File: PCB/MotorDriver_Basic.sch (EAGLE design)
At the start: 20 parts, among them J2 MTR_CTRL, J3 MCU PWR, J4 MTR PWR

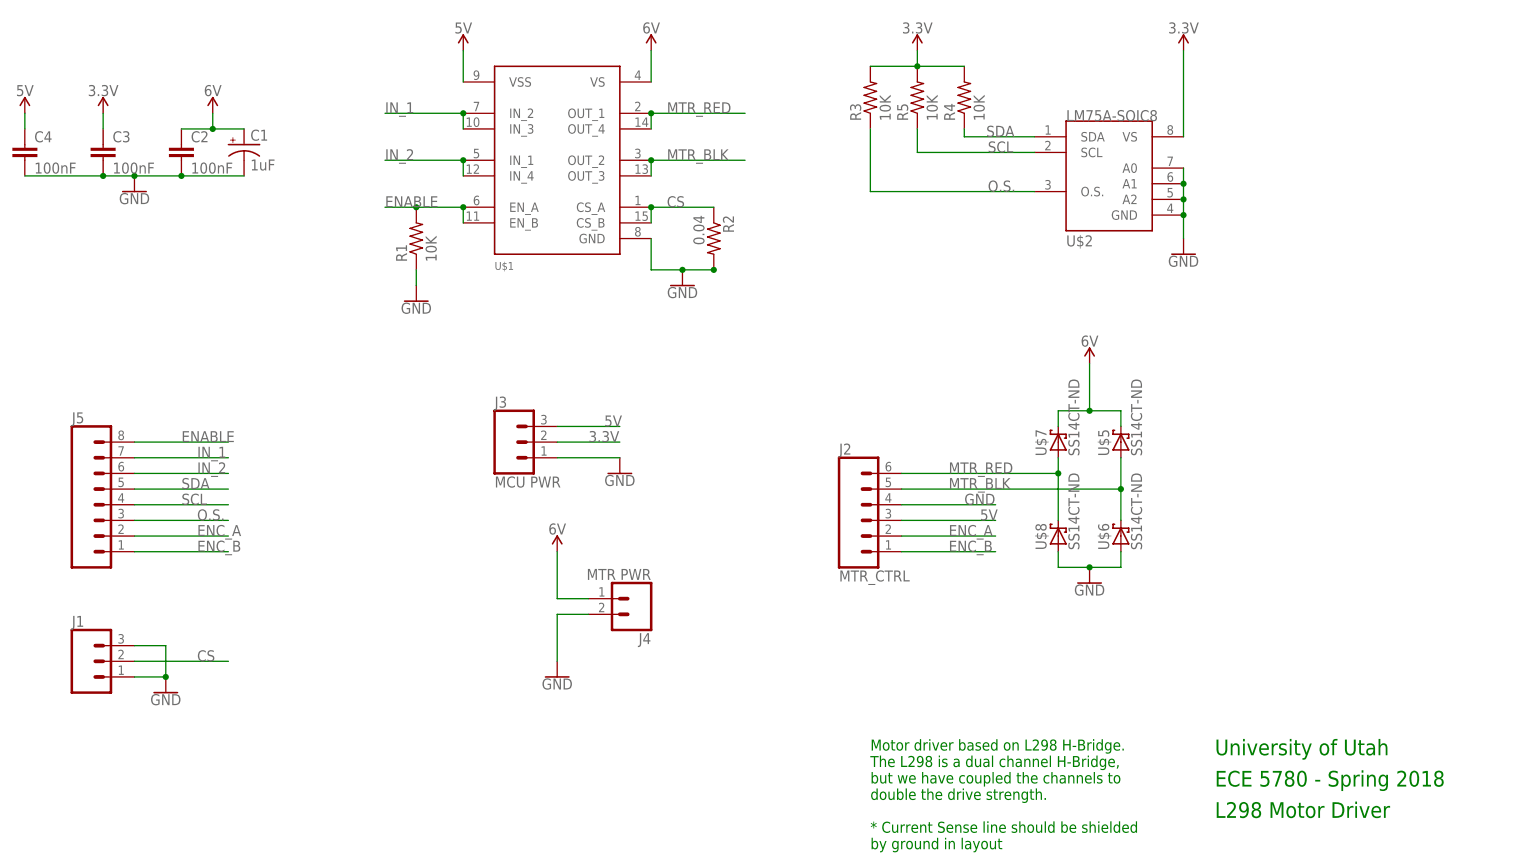
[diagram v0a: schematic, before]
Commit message: added the motor driver to schematic.
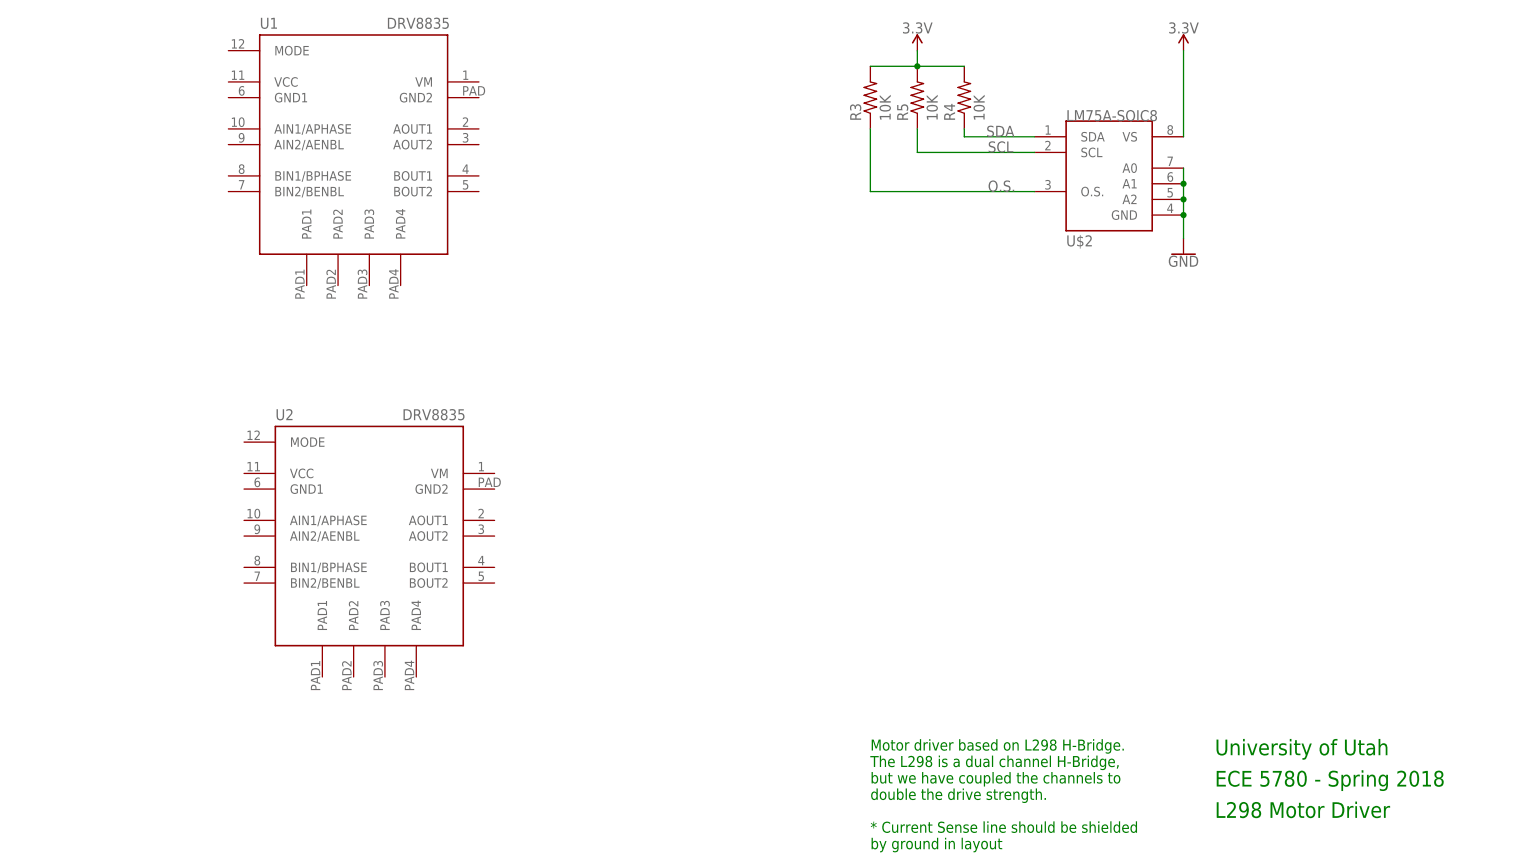
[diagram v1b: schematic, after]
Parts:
- removed C1: 1uF, rcl:CPOL-USE2.5-6
- removed C2, C3, C4: 100nF, rcl:C-EUC1206
- removed J1: (no value), SparkFun-Connectors:CONN_03
- removed J2: MTR_CTRL, SparkFun-Connectors:CONN_06SILK_FEMALE_PTH
- removed J3: MCU PWR, SparkFun-Connectors:CONN_03
- removed J4: MTR PWR, L298_Motor_Driver_Lib_ECE5780:CONN2-5MM-SCREW-TERM
- removed J5: (no value), SparkFun-Connectors:CONN_08"
- removed R1: 10K, rcl:R-US_M1206
- removed R2: 0.04, rcl:R-US_M1206
- removed U$1: L298N-MULTIWATT15, ECE5780-MotorDriver:L298N-MULTIWATT15
- removed U$5, U$6, U$7, U$8: SS14CT-ND, L298_Motor_Driver_Lib_ECE5780:SS14CT-ND
- added U1, U2: DRV8835, bt_motordriver:DRV8835
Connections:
- removed net 5V: C4.1, J2.3, J3.3, U$1.VSS
- removed net CS: J1.2, R2.1, U$1.CS_A, U$1.CS_B
- removed net ENABLE: J5.8, R1.2, U$1.EN_A, U$1.EN_B
- removed net ENC_A: J2.2, J5.2
- removed net ENC_B: J2.1, J5.1
- removed net IN_1: J5.7, U$1.IN_2, U$1.IN_3
- removed net IN_2: J5.6, U$1.IN_1, U$1.IN_4
- removed net MTR_BLK: J2.5, U$1.OUT_2, U$1.OUT_3, U$5.A, U$6.C
- removed net MTR_RED: J2.6, U$1.OUT_1, U$1.OUT_4, U$7.A, U$8.C
- removed net VCC: C1.+, C2.1, J4.1, U$1.VS, U$5.C, U$7.C
- net 3.3V: no longer C3.1, J3.2
- net GND: no longer C1.-, C2.2, C3.2, C4.2, J1.1, J1.3, J2.4, J3.1, J4.2, R1.1, R2.2, U$1.GND, U$6.A, U$8.A
- net O.S.: no longer J5.3
- net SCL: no longer J5.4
- net SDA: no longer J5.5

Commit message: Finished the Schematic.
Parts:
- removed U2: DRV8835, bt_motordriver:DRV8835
- added C1, C2, C3, C5: 0.1 uF, rcl:C-EUC1206
- added C4: 2.2 nF, rcl:C-EUC1206
- added C6: 1.0 uF, rcl:C-US025-050X050
- added C7: 10 nF, rcl:C-EUC1206
- added IC1: MPU6050, invensense:MPU6050
- added JP1, JP2: (no value), pinhead:PINHD-1X8
- added R1: 0, rcl:R-US_M1206
- added R2: 10K, rcl:R-US_M1206
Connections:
- removed net 3.3V: R3.2, R4.2, R5.2, U$2.VS
- new net AIN1: JP2.1, U1.AIN1/APHASE
- new net AIN2: JP2.2, U1.AIN2/AENBL
- new net BIN1: JP2.3, U1.BIN1/BPHASE
- new net BIN2: JP2.4, U1.BIN2/BENBL
- new net IMU_INT: JP1.3, R1.2, R2.1
- new net MOUTA1: JP2.8, U1.AOUT1
- new net MOUTA2: JP2.7, U1.AOUT2
- new net MOUTB1: JP1.8, U1.BOUT1
- new net MOUTB2: JP1.7, U1.BOUT2
- new net N$1: C4.1, IC1G$1.CPOUT
- new net N$2: IC1G$1.INT, R1.1
- new net REGOUT: C2.1, IC1G$1.REGOUT
- new net VCC: C3.1, C7.1, IC1G$1.VLOGIC, JP2.6, R2.2, R3.2, R4.2, R5.2, U$2.VS, U1.VCC
- new net VM: C1.1, C5.1, C6.1, IC1G$1.VDD, JP2.5, U1.VM
- net GND: now also C1.2, C2.2, C3.2, C4.2, C5.2, C6.2, C7.2, IC1G$1.AD0, IC1G$1.AUX_CL, IC1G$1.AUX_DA, IC1G$1.CLKIN, IC1G$1.FSYNC, IC1G$1.GND, IC1G$1.GND@1, JP1.1, JP1.2, JP1.4, U1.GND1, U1.GND2, U1.MODE, U1.PAD1, U1.PAD2, U1.PAD3, U1.PAD4
- net SCL: now also IC1G$1.SCL, JP1.6
- net SDA: now also IC1G$1.SDA, JP1.5

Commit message: Tweaked the board file
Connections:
- net AIN1: now also JP2.4; no longer JP2.1
- net AIN2: now also JP2.3; no longer JP2.2
- net BIN1: now also JP2.2; no longer JP2.3
- net BIN2: now also JP2.1; no longer JP2.4
- net GND: now also JP1.5, JP2.5, JP2.6; no longer JP1.1, JP1.2, JP1.4
- net IMU_INT: now also JP1.8; no longer JP1.3
- net MOUTA1: now also JP1.4; no longer JP2.8
- net MOUTA2: now also JP1.3; no longer JP2.7
- net MOUTB1: now also JP1.2; no longer JP1.8
- net MOUTB2: now also JP1.1; no longer JP1.7
- net SCL: now also JP2.7; no longer JP1.6
- net SDA: now also JP2.8; no longer JP1.5
- net VCC: now also JP1.7; no longer JP2.6
- net VM: now also JP1.6; no longer JP2.5
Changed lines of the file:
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@@
 </segment>
 <segment>
-<wire x1="40.64" y1="86.36" x2="48.26" y2="86.36" width="0.1524" layer="91"/>
-<pinref part="JP1" gate="A" pin="4"/>
-<label x="48.26" y="86.36" size="1.778" layer="95"/>
-</segment>
-<segment>
-<wire x1="40.64" y1="81.28" x2="48.26" y2="81.28" width="0.1524" layer="91"/>
-<pinref part="JP1" gate="A" pin="2"/>
-<label x="48.26" y="81.28" size="1.778" layer="95"/>
-</segment>
-<segment>
-<wire x1="40.64" y1="78.74" x2="48.26" y2="78.74" width="0.1524" layer="91"/>
-<pinref part="JP1" gate="A" pin="1"/>
-<label x="48.26" y="78.74" size="1.778" layer="95"/>
+<wire x1="40.64" y1="60.96" x2="48.26" y2="60.96" width="0.1524" layer="91"/>
+<pinref part="JP2" gate="A" pin="5"/>
+<label x="48.26" y="60.96" size="1.778" layer="95"/>
+</segment>
+<segment>
+<wire x1="40.64" y1="88.9" x2="48.26" y2="88.9" width="0.1524" layer="91"/>
+<pinref part="JP1" gate="A" pin="5"/>
+<label x="48.26" y="88.9" size="1.778" layer="95"/>
+</segment>
+<segment>
+<wire x1="40.64" y1="63.5" x2="48.26" y2="63.5" width="0.1524" layer="91"/>
+<pinref part="JP2" gate="A" pin="6"/>
+<label x="48.26" y="63.5" size="1.778" layer="95"/>
 </segment>
 </net>
@@
 </segment>
 <segment>
-<wire x1="40.64" y1="88.9" x2="48.26" y2="88.9" width="0.1524" layer="91"/>
-<pinref part="JP1" gate="A" pin="5"/>
-<label x="48.26" y="88.9" size="1.778" layer="95"/>
+<wire x1="40.64" y1="68.58" x2="48.26" y2="68.58" width="0.1524" layer="91"/>
+<pinref part="JP2" gate="A" pin="8"/>
+<label x="48.26" y="68.58" size="1.778" layer="95"/>
 </segment>
 </net>
@@
 </segment>
 <segment>
-<wire x1="40.64" y1="91.44" x2="48.26" y2="91.44" width="0.1524" layer="91"/>
-<pinref part="JP1" gate="A" pin="6"/>
-<label x="48.26" y="91.44" size="1.778" layer="95"/>
+<wire x1="40.64" y1="66.04" x2="48.26" y2="66.04" width="0.1524" layer="91"/>
+<pinref part="JP2" gate="A" pin="7"/>
+<label x="48.26" y="66.04" size="1.778" layer="95"/>
 </segment>
 </net>
@@
 </segment>
 <segment>
-<wire x1="40.64" y1="63.5" x2="48.26" y2="63.5" width="0.1524" layer="91"/>
-<pinref part="JP2" gate="A" pin="6"/>
-<label x="48.26" y="63.5" size="1.778" layer="95"/>
+<wire x1="40.64" y1="93.98" x2="48.26" y2="93.98" width="0.1524" layer="91"/>
+<pinref part="JP1" gate="A" pin="7"/>
+<label x="48.26" y="93.98" size="1.778" layer="95"/>
 </segment>
 </net>
@@
 </segment>
 <segment>
-<wire x1="40.64" y1="60.96" x2="48.26" y2="60.96" width="0.1524" layer="91"/>
-<pinref part="JP2" gate="A" pin="5"/>
-<label x="48.26" y="60.96" size="1.778" layer="95"/>
+<wire x1="40.64" y1="91.44" x2="48.26" y2="91.44" width="0.1524" layer="91"/>
+<pinref part="JP1" gate="A" pin="6"/>
+<label x="48.26" y="91.44" size="1.778" layer="95"/>
 </segment>
 </net>
@@
 </segment>
 <segment>
+<wire x1="40.64" y1="58.42" x2="48.26" y2="58.42" width="0.1524" layer="91"/>
+<pinref part="JP2" gate="A" pin="4"/>
+<label x="48.26" y="58.42" size="1.778" layer="95"/>
+</segment>
+</net>
+<net name="BIN2" class="0">
+<segment>
+<pinref part="U1" gate="G$1" pin="BIN2/BENBL"/>
+<wire x1="58.42" y1="111.76" x2="50.8" y2="111.76" width="0.1524" layer="91"/>
+<label x="48.26" y="111.76" size="1.778" layer="95"/>
+</segment>
+<segment>
 <pinref part="JP2" gate="A" pin="1"/>
 <wire x1="40.64" y1="50.8" x2="48.26" y2="50.8" width="0.1524" layer="91"/>
@@
 </segment>
 </net>
-<net name="BIN2" class="0">
-<segment>
-<pinref part="U1" gate="G$1" pin="BIN2/BENBL"/>
-<wire x1="58.42" y1="111.76" x2="50.8" y2="111.76" width="0.1524" layer="91"/>
-<label x="48.26" y="111.76" size="1.778" layer="95"/>
-</segment>
-<segment>
-<wire x1="40.64" y1="58.42" x2="48.26" y2="58.42" width="0.1524" layer="91"/>
-<pinref part="JP2" gate="A" pin="4"/>
-<label x="48.26" y="58.42" size="1.778" layer="95"/>
-</segment>
-</net>
 <net name="MOUTA1" class="0">
 <segment>
@@
 </segment>
 <segment>
-<wire x1="40.64" y1="68.58" x2="48.26" y2="68.58" width="0.1524" layer="91"/>
-<pinref part="JP2" gate="A" pin="8"/>
-<label x="48.26" y="68.58" size="1.778" layer="95"/>
+<wire x1="40.64" y1="86.36" x2="48.26" y2="86.36" width="0.1524" layer="91"/>
+<pinref part="JP1" gate="A" pin="4"/>
+<label x="48.26" y="86.36" size="1.778" layer="95"/>
 </segment>
 </net>
@@
 </segment>
 <segment>
-<wire x1="40.64" y1="66.04" x2="48.26" y2="66.04" width="0.1524" layer="91"/>
-<pinref part="JP2" gate="A" pin="7"/>
-<label x="48.26" y="66.04" size="1.778" layer="95"/>
+<wire x1="40.64" y1="83.82" x2="48.26" y2="83.82" width="0.1524" layer="91"/>
+<pinref part="JP1" gate="A" pin="3"/>
+<label x="48.26" y="83.82" size="1.778" layer="95"/>
 </segment>
 </net>
@@
 </segment>
 <segment>
-<wire x1="40.64" y1="96.52" x2="48.26" y2="96.52" width="0.1524" layer="91"/>
-<pinref part="JP1" gate="A" pin="8"/>
-<label x="48.26" y="96.52" size="1.778" layer="95"/>
+<wire x1="40.64" y1="81.28" x2="48.26" y2="81.28" width="0.1524" layer="91"/>
+<pinref part="JP1" gate="A" pin="2"/>
+<label x="48.26" y="81.28" size="1.778" layer="95"/>
 </segment>
 </net>
@@
 </segment>
 <segment>
-<wire x1="40.64" y1="93.98" x2="48.26" y2="93.98" width="0.1524" layer="91"/>
-<pinref part="JP1" gate="A" pin="7"/>
-<label x="48.26" y="93.98" size="1.778" layer="95"/>
+<wire x1="40.64" y1="78.74" x2="48.26" y2="78.74" width="0.1524" layer="91"/>
+<pinref part="JP1" gate="A" pin="1"/>
+<label x="48.26" y="78.74" size="1.778" layer="95"/>
 </segment>
 </net>
@@
 </segment>
 <segment>
-<wire x1="40.64" y1="83.82" x2="48.26" y2="83.82" width="0.1524" layer="91"/>
-<pinref part="JP1" gate="A" pin="3"/>
-<label x="48.26" y="83.82" size="1.778" layer="95"/>
+<wire x1="40.64" y1="96.52" x2="48.26" y2="96.52" width="0.1524" layer="91"/>
+<pinref part="JP1" gate="A" pin="8"/>
+<label x="48.26" y="96.52" size="1.778" layer="95"/>
 </segment>
 </net>
@@
 </segment>
 <segment>
+<wire x1="40.64" y1="53.34" x2="48.26" y2="53.34" width="0.1524" layer="91"/>
+<pinref part="JP2" gate="A" pin="2"/>
+<label x="48.26" y="53.34" size="1.778" layer="95"/>
+</segment>
+</net>
+<net name="AIN2" class="0">
+<segment>
+<pinref part="U1" gate="G$1" pin="AIN2/AENBL"/>
+<wire x1="58.42" y1="119.38" x2="50.8" y2="119.38" width="0.1524" layer="91"/>
+<label x="48.26" y="119.38" size="1.778" layer="95"/>
+</segment>
+<segment>
 <wire x1="40.64" y1="55.88" x2="48.26" y2="55.88" width="0.1524" layer="91"/>
 <pinref part="JP2" gate="A" pin="3"/>
@@
 </segment>
 </net>
-<net name="AIN2" class="0">
-<segment>
-<pinref part="U1" gate="G$1" pin="AIN2/AENBL"/>
-<wire x1="58.42" y1="119.38" x2="50.8" y2="119.38" width="0.1524" layer="91"/>
-<label x="48.26" y="119.38" size="1.778" layer="95"/>
-</segment>
-<segment>
-<wire x1="40.64" y1="53.34" x2="48.26" y2="53.34" width="0.1524" layer="91"/>
-<pinref part="JP2" gate="A" pin="2"/>
-<label x="48.26" y="53.34" size="1.778" layer="95"/>
-</segment>
-</net>

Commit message: Tweaked schematic/Created board
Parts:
- removed R1: 0, rcl:R-US_M1206
- removed R2: 10K, rcl:R-US_M1206
- R4, R5: value 10K -> 3.3K
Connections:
- removed net N$2: IC1G$1.INT, R1.1
- net IMU_INT: now also IC1G$1.INT; no longer R1.2, R2.1
- net VCC: now also C5.1, IC1G$1.VDD; no longer R2.2
- net VM: no longer C5.1, IC1G$1.VDD
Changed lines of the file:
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@@
 <parts>
 <part name="R3" library="rcl" library_urn="urn:adsk.eagle:library:334" deviceset="R-US_" device="M1206" package3d_urn="urn:adsk.eagle:package:23566/1" value="10K"/>
-<part name="R4" library="rcl" library_urn="urn:adsk.eagle:library:334" deviceset="R-US_" device="M1206" package3d_urn="urn:adsk.eagle:package:23566/1" value="10K"/>
-<part name="R5" library="rcl" library_urn="urn:adsk.eagle:library:334" deviceset="R-US_" device="M1206" package3d_urn="urn:adsk.eagle:package:23566/1" value="10K"/>
+<part name="R4" library="rcl" library_urn="urn:adsk.eagle:library:334" deviceset="R-US_" device="M1206" package3d_urn="urn:adsk.eagle:package:23566/1" value="3.3K"/>
+<part name="R5" library="rcl" library_urn="urn:adsk.eagle:library:334" deviceset="R-US_" device="M1206" package3d_urn="urn:adsk.eagle:package:23566/1" value="3.3K"/>
 <part name="U$2" library="L298_Motor_Driver_Lib_ECE5780" deviceset="LM75A-SOIC8" device=""/>
 <part name="GND5" library="SparkFun-PowerSymbols" library_urn="urn:adsk.eagle:library:530" deviceset="GND" device=""/>
@@
 <part name="C5" library="rcl" library_urn="urn:adsk.eagle:library:334" deviceset="C-EU" device="C1206" package3d_urn="urn:adsk.eagle:package:23618/2" value="0.1 uF"/>
 <part name="C7" library="rcl" library_urn="urn:adsk.eagle:library:334" deviceset="C-EU" device="C1206" package3d_urn="urn:adsk.eagle:package:23618/2" value="10 nF"/>
-<part name="R1" library="rcl" library_urn="urn:adsk.eagle:library:334" deviceset="R-US_" device="M1206" package3d_urn="urn:adsk.eagle:package:23566/1" value="0"/>
-<part name="R2" library="rcl" library_urn="urn:adsk.eagle:library:334" deviceset="R-US_" device="M1206" package3d_urn="urn:adsk.eagle:package:23566/1" value="10K"/>
 <part name="JP1" library="pinhead" library_urn="urn:adsk.eagle:library:325" deviceset="PINHD-1X8" device="" package3d_urn="urn:adsk.eagle:package:22409/2"/>
 <part name="JP2" library="pinhead" library_urn="urn:adsk.eagle:library:325" deviceset="PINHD-1X8" device="" package3d_urn="urn:adsk.eagle:package:22409/2"/>
@@
 <attribute name="VALUE" x="170.815" y="67.945" size="1.778" layer="96"/>
 </instance>
-<instance part="SUPPLY7" gate="GND" x="165.1" y="43.18" smashed="yes">
-<attribute name="VALUE" x="163.195" y="40.005" size="1.778" layer="96"/>
+<instance part="SUPPLY7" gate="GND" x="165.1" y="40.64" smashed="yes">
+<attribute name="VALUE" x="163.195" y="37.465" size="1.778" layer="96"/>
 </instance>
 <instance part="SUPPLY9" gate="GND" x="119.38" y="58.42" smashed="yes">
@@
 <attribute name="NAME" x="176.784" y="51.181" size="1.778" layer="95"/>
 <attribute name="VALUE" x="176.784" y="46.101" size="1.778" layer="96"/>
-</instance>
-<instance part="R1" gate="G$1" x="104.14" y="55.88" smashed="yes" rot="R180">
-<attribute name="NAME" x="107.95" y="54.3814" size="1.778" layer="95" rot="R180"/>
-<attribute name="VALUE" x="107.95" y="59.182" size="1.778" layer="96" rot="R180"/>
-</instance>
-<instance part="R2" gate="G$1" x="96.52" y="60.96" smashed="yes" rot="R90">
-<attribute name="NAME" x="95.0214" y="57.15" size="1.778" layer="95" rot="R90"/>
-<attribute name="VALUE" x="99.822" y="57.15" size="1.778" layer="96" rot="R90"/>
 </instance>
 <instance part="JP1" gate="A" x="38.1" y="88.9" smashed="yes" rot="R180">
@@
 </segment>
 <segment>
+<pinref part="IC1" gate="G$1" pin="GND"/>
+<wire x1="165.1" y1="48.26" x2="162.56" y2="48.26" width="0.1524" layer="91"/>
+<wire x1="165.1" y1="48.26" x2="165.1" y2="43.18" width="0.1524" layer="91"/>
+<pinref part="SUPPLY7" gate="GND" pin="GND"/>
 <pinref part="IC1" gate="G$1" pin="GND@1"/>
 <wire x1="162.56" y1="50.8" x2="165.1" y2="50.8" width="0.1524" layer="91"/>
 <wire x1="165.1" y1="50.8" x2="165.1" y2="48.26" width="0.1524" layer="91"/>
-<pinref part="IC1" gate="G$1" pin="GND"/>
-<wire x1="165.1" y1="48.26" x2="162.56" y2="48.26" width="0.1524" layer="91"/>
-<wire x1="165.1" y1="48.26" x2="165.1" y2="45.72" width="0.1524" layer="91"/>
-<pinref part="SUPPLY7" gate="GND" pin="GND"/>
+<junction x="165.1" y="48.26"/>
 </segment>
 <segment>
@@
 <segment>
 <pinref part="IC1" gate="G$1" pin="VLOGIC"/>
-<wire x1="162.56" y1="53.34" x2="175.26" y2="53.34" width="0.1524" layer="91"/>
+<wire x1="162.56" y1="53.34" x2="167.64" y2="53.34" width="0.1524" layer="91"/>
 <label x="170.18" y="53.34" size="1.778" layer="95"/>
 <pinref part="C7" gate="G$1" pin="1"/>
-</segment>
-<segment>
-<pinref part="R2" gate="G$1" pin="2"/>
-<wire x1="96.52" y1="66.04" x2="96.52" y2="68.58" width="0.1524" layer="91"/>
-<label x="96.52" y="68.58" size="1.778" layer="95"/>
+<pinref part="IC1" gate="G$1" pin="VDD"/>
+<pinref part="C5" gate="G$1" pin="1"/>
+<wire x1="167.64" y1="53.34" x2="175.26" y2="53.34" width="0.1524" layer="91"/>
+<wire x1="162.56" y1="55.88" x2="167.64" y2="55.88" width="0.1524" layer="91"/>
+<wire x1="167.64" y1="55.88" x2="182.88" y2="55.88" width="0.1524" layer="91"/>
+<wire x1="167.64" y1="53.34" x2="167.64" y2="55.88" width="0.1524" layer="91"/>
+<junction x="167.64" y="53.34"/>
+<junction x="167.64" y="55.88"/>
 </segment>
 <segment>
@@
 </segment>
 <segment>
-<pinref part="IC1" gate="G$1" pin="VDD"/>
-<label x="170.18" y="55.88" size="1.778" layer="95"/>
-<pinref part="C5" gate="G$1" pin="1"/>
-<wire x1="162.56" y1="55.88" x2="182.88" y2="55.88" width="0.1524" layer="91"/>
-</segment>
-<segment>
 <wire x1="40.64" y1="91.44" x2="48.26" y2="91.44" width="0.1524" layer="91"/>
 <pinref part="JP1" gate="A" pin="6"/>
@@
 </segment>
 </net>
-<net name="N$2" class="0">
-<segment>
+<net name="IMU_INT" class="0">
+<segment>
+<label x="101.6" y="55.88" size="1.778" layer="95"/>
 <pinref part="IC1" gate="G$1" pin="INT"/>
-<wire x1="121.92" y1="55.88" x2="109.22" y2="55.88" width="0.1524" layer="91"/>
-<pinref part="R1" gate="G$1" pin="1"/>
-</segment>
-</net>
-<net name="IMU_INT" class="0">
-<segment>
-<pinref part="R1" gate="G$1" pin="2"/>
-<wire x1="99.06" y1="55.88" x2="96.52" y2="55.88" width="0.1524" layer="91"/>
-<label x="83.82" y="55.88" size="1.778" layer="95"/>
-<pinref part="R2" gate="G$1" pin="1"/>
-<wire x1="96.52" y1="55.88" x2="93.98" y2="55.88" width="0.1524" layer="91"/>
-<junction x="96.52" y="55.88"/>
-</segment>
-<segment>
+<wire x1="111.76" y1="55.88" x2="121.92" y2="55.88" width="0.1524" layer="91"/>
+</segment>
+<segment>
